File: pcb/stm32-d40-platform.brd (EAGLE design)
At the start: 99.1 x 99.1 mm, 84 parts, among them IC1 STM32F103C8, IC2 TODO AMIS30663CANG2G, IC3 STM32F103C8, J1 DIP-40, Q1 8MHz, Q2 8MHz, SW1 KSS-2EG4430, SW2 KSS-2EG4430, X1 DG3XX-03-3.5

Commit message: motherboard in progress
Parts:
- added 3V3, AVCC, PA0, PA1, PA10, PA11, PA12, PA13, PA14, PA15, PA2, PA3, PA4, PA5, PA6, PA7, PA8, PA9, PB0, PB1, PB10, PB11, PB12, PB13, PB14, PB15, PB2, PB3, PB4, PB5, PB6, PB7, PB8, PB9, PC14, PC15, RST, VBAT: (no value), pinhead-fixdrills:1X01
- added C23, C24: 22pF, rc-master-smd:C0603
- added G1: B2430, battery:B2430
- added IC4: (no value), transistor-arrays:SO16
- added K1, K2, K3, K4: ZNS5124, myrelays:ZN5
- added MOD1: STM32-MOD-CAN, stamp:DIL40
- added Q3: 32768Hz, crystal:TC38H-G
- added R36: 1M, rc-master-smd:R0603
- added SG1: F/QMBIII, buzzer:F/QMBIII
- added X2: DG3XX-12-5.0, degson:DG306-5.0-12P
- added X3: DG3XX-02-5.0, degson:DG306-5.0-02P
- moved U$1 58.4 mm to (93.6, 86.6)
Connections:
- new net !S2.RESET: MOD1.9, RST.1
- new net N$366: IC4.15, K4.A2
- new net N$367: IC4.14, K3.A2
- new net N$368: IC4.13, K2.A2
- new net N$369: IC4.12, K1.A2
- new net N$370: IC4.16, SG1.-
- new net N$64: K1.14, X2.1
- new net N$65: K1.11, X2.2
- new net N$66: K1.12, X2.3
- new net N$67: K2.14, X2.4
- new net N$68: K2.11, X2.5
- new net N$69: K2.12, X2.6
- new net N$70: K3.14, X2.7
- new net N$71: K3.11, X2.8
- new net N$72: K3.12, X2.9
- new net N$73: K4.14, X2.10
- new net N$74: K4.11, X2.11
- new net N$75: K4.12, X2.12
- new net S2.3V3: 3V3.1, MOD1.10
- new net S2.AVCC: AVCC.1, MOD1.30
- new net S2.OSC32_IN: C24.1, MOD1.13, PC14.1, Q3.2, R36.2
- new net S2.OSC32_OUT: C23.1, MOD1.12, PC15.1, Q3.1, R36.1
- new net S2.PA0: MOD1.40, PA0.1
- new net S2.PA1: MOD1.39, PA1.1
- new net S2.PA10: MOD1.24, PA10.1
- new net S2.PA11: MOD1.25, PA11.1
- new net S2.PA12: MOD1.26, PA12.1
- new net S2.PA13: MOD1.27, PA13.1
- new net S2.PA14: MOD1.28, PA14.1
- new net S2.PA15: MOD1.29, PA15.1
- new net S2.PA2: MOD1.38, PA2.1
- new net S2.PA3: MOD1.37, PA3.1
- new net S2.PA4: MOD1.36, PA4.1
- new net S2.PA5: MOD1.35, PA5.1
- new net S2.PA6: MOD1.34, PA6.1
- new net S2.PA7: MOD1.33, PA7.1
- new net S2.PA8: MOD1.22, PA8.1
- new net S2.PA9: MOD1.23, PA9.1
- new net S2.PB0: MOD1.1, PB0.1
- new net S2.PB1: MOD1.2, PB1.1
- new net S2.PB10: MOD1.16, PB10.1
- new net S2.PB11: MOD1.17, PB11.1
- new net S2.PB12: MOD1.18, PB12.1
- new net S2.PB13: MOD1.19, PB13.1
- new net S2.PB14: MOD1.20, PB14.1
- new net S2.PB15: MOD1.21, PB15.1
- new net S2.PB2: MOD1.3, PB2.1
- new net S2.PB3: MOD1.4, PB3.1
- new net S2.PB4: MOD1.5, PB4.1
- new net S2.PB5: MOD1.6, PB5.1
- new net S2.PB6: MOD1.7, PB6.1
- new net S2.PB7: MOD1.8, PB7.1
- new net S2.PB8: MOD1.14, PB8.1
- new net S2.PB9: MOD1.15, PB9.1
- new net S2.VBAT: G1.+, MOD1.32, VBAT.1
- net +5V: now also IC4.9, K1.A1, K2.A1, K3.A1, K4.A1, SG1.+, X3.2
- net GND: now also C23.2, C24.2, G1.-, IC4.8, MOD1.11, MOD1.31, Q3.GND, X3.1
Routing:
- net GND: track 5.08 -> 340.3 mm, vias 91 -> 144
- net S2.3V3: track 0.00 -> 257.6 mm, vias 0 -> 50
- net +5V: track 11.5 -> 77.2 mm
- net N$74: track 0.00 -> 30.8 mm
- net N$65: track 0.00 -> 30.8 mm
- net N$71: track 0.00 -> 28.1 mm
- net N$68: track 0.00 -> 28.1 mm
- net S2.OSC32_IN: track 0.00 -> 18.5 mm
- net N$75: track 0.00 -> 17.8 mm
- net S2.OSC32_OUT: track 0.00 -> 17.7 mm
- net N$64: track 0.00 -> 17.6 mm
- net N$73: track 0.00 -> 15.6 mm
- net N$66: track 0.00 -> 15.4 mm
- net N$72: track 0.00 -> 15.1 mm
- net N$67: track 0.00 -> 14.9 mm
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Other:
- outline, holes or cut-outs redrawn

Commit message: PCB ready
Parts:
- removed SG1: F/QMBIII, buzzer:F/QMBIII
- added C25, C26: 0.1, rc-master-smd:C0805
- added C27, C28: 100uF/6V3, rc-master:CE-035X080
- added D3: (no value), diodes:SMB
- added IN1, IN2, IN3, IN4, IN5, IN6, IN7, OUT5, OUT6, OUT7: (no value), pinhead-fixdrills:1X01
- added U2: (no value), vreg-linear:SOT223
- C23, C24: device rc-master-smd:C0603 -> rc-master-smd:C0805
- R36: device rc-master-smd:R0603 -> rc-master-smd:R0805
- moved U$1 21.7 mm to (72.4, 91.4)
- moved IC4 5.24 mm to (80.0, 69.8), turned to 0 degrees
- moved X3 2.54 mm to (85.1, 94.0)
- moved C23 0.63 mm to (34.3, 47.6)
- moved C24 0.63 mm to (36.8, 47.6)
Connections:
- removed net N$370: IC4.16, SG1.-
- new net HEAT: U2.4
- new net N$11: D3.A, X3.2
- new net S2.IN1: IC4.1, IN1.1
- new net S2.IN2: IC4.2, IN2.1
- new net S2.IN3: IC4.3, IN3.1
- new net S2.IN4: IC4.4, IN4.1
- new net S2.IN5: IC4.5, IN5.1
- new net S2.IN6: IC4.6, IN6.1
- new net S2.IN7: IC4.7, IN7.1
- new net S2.OUT5: IC4.12, OUT5.1
- new net S2.OUT6: IC4.11, OUT6.1
- new net S2.OUT7: IC4.10, OUT7.1
- net +5V: now also C25.1, C27.+, D3.C, U2.3; no longer SG1.+, X3.2
- net GND: now also C25.2, C26.2, C27.-, C28.-, U2.1
- net N$366: now also IC4.13; no longer IC4.15
- net N$368: now also IC4.15; no longer IC4.13
- net N$369: now also IC4.16; no longer IC4.12
- net S2.3V3: now also C26.1, C28.+, U2.2
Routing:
- net N$366: track 0.00 -> 80.5 mm, vias 0 -> 1
- net +5V: track 77.2 -> 143.7 mm, vias 1 -> 5
- net N$367: track 0.00 -> 60.4 mm, vias 0 -> 1
- net GND: track 340.3 -> 397.7 mm
- net S2.PB12: track 5.08 -> 45.7 mm, vias 0 -> 2
- net N$368: track 0.00 -> 40.3 mm, vias 0 -> 1
- net S2.PB14: track 5.08 -> 45.3 mm, vias 0 -> 2
- net S2.PB13: track 5.08 -> 44.5 mm, vias 0 -> 2
- net S2.PB15: track 5.08 -> 33.7 mm, vias 0 -> 2
- net S2.3V3: track 257.6 -> 280.1 mm, vias 50 -> 49
- net N$369: track 0.00 -> 20.2 mm, vias 0 -> 1
- net S2.OUT7: track 0.00 -> 12.5 mm
- net S2.OUT6: track 0.00 -> 11.8 mm
- net S2.OUT5: track 0.00 -> 11.7 mm
- net N$11: track 0.00 -> 8.22 mm
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- added copper zone on layer 1, net HEAT
- added copper zone on layer 16, net HEAT

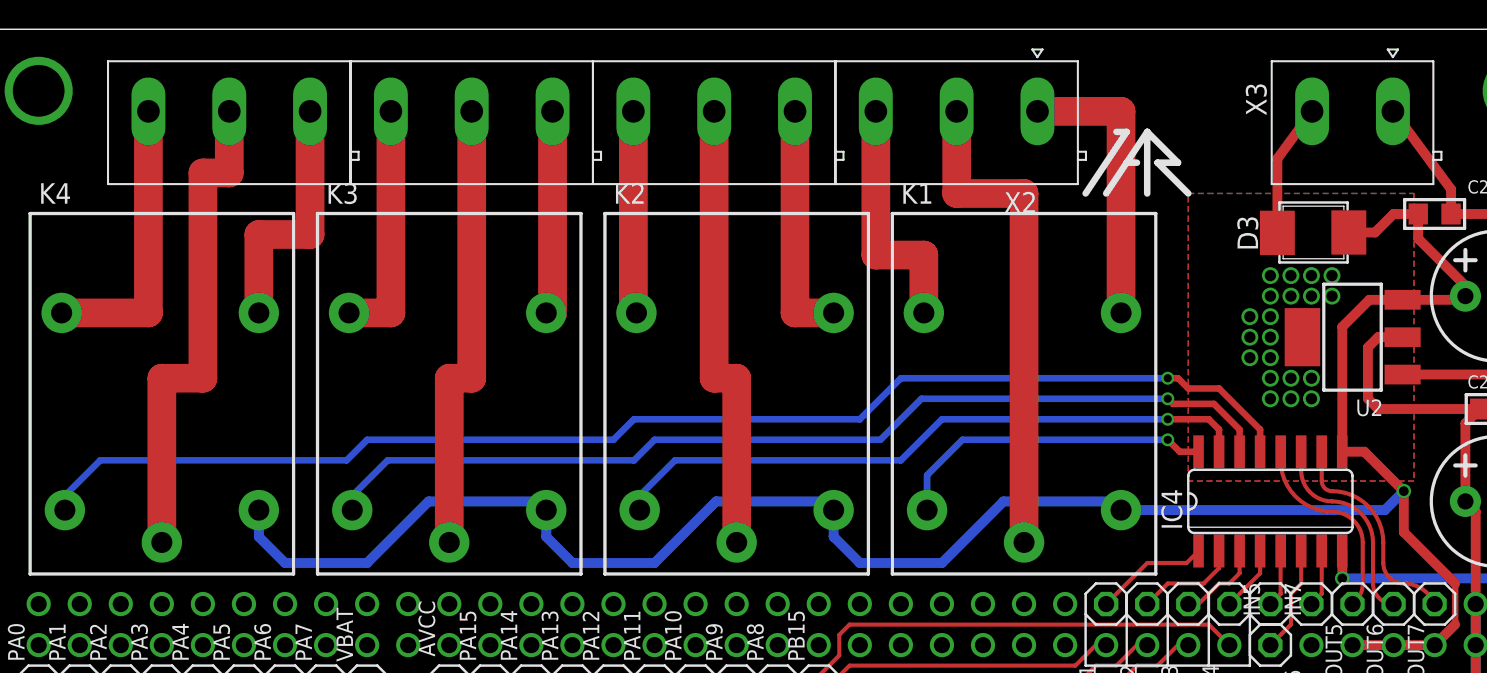
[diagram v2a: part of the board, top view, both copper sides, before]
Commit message: stm32-40 ready to production PCB. some changes in platform
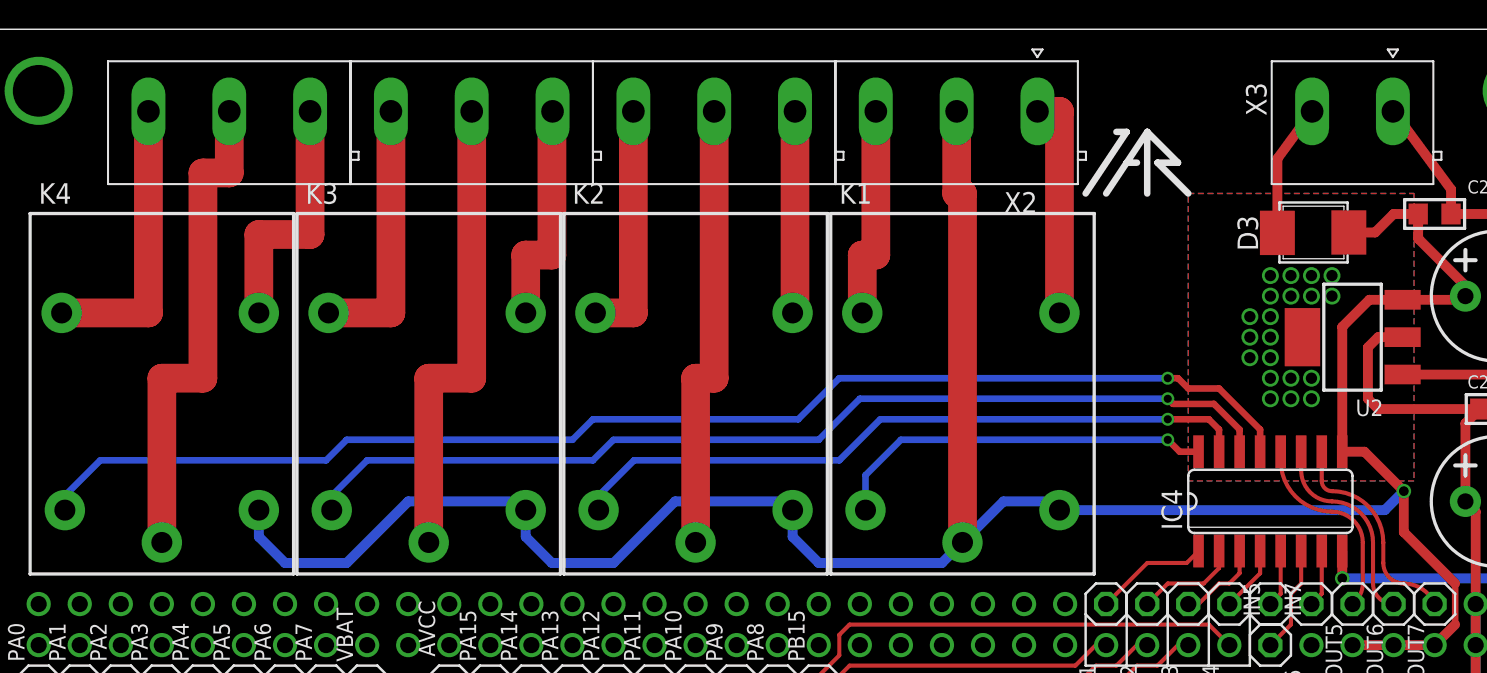
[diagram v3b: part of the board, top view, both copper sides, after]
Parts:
- moved K1 3.81 mm to (61.0, 76.2)
- moved K2 2.54 mm to (44.5, 76.2)
- moved K3 1.27 mm to (27.9, 76.2)
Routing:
- net N$64: track 17.6 -> 13.8 mm
- net N$369: track 20.2 -> 24.0 mm
- net N$65: track 30.8 -> 27.0 mm
- net N$368: track 40.3 -> 42.9 mm
- net N$67: track 14.9 -> 12.6 mm
- net N$69: track 12.7 -> 14.8 mm
- net N$66: track 15.4 -> 13.3 mm
- net N$72: track 15.1 -> 16.3 mm
- net N$70: track 12.9 -> 14.1 mm
- net N$71: track 28.1 -> 29.3 mm
- net N$367: track 60.4 -> 61.7 mm

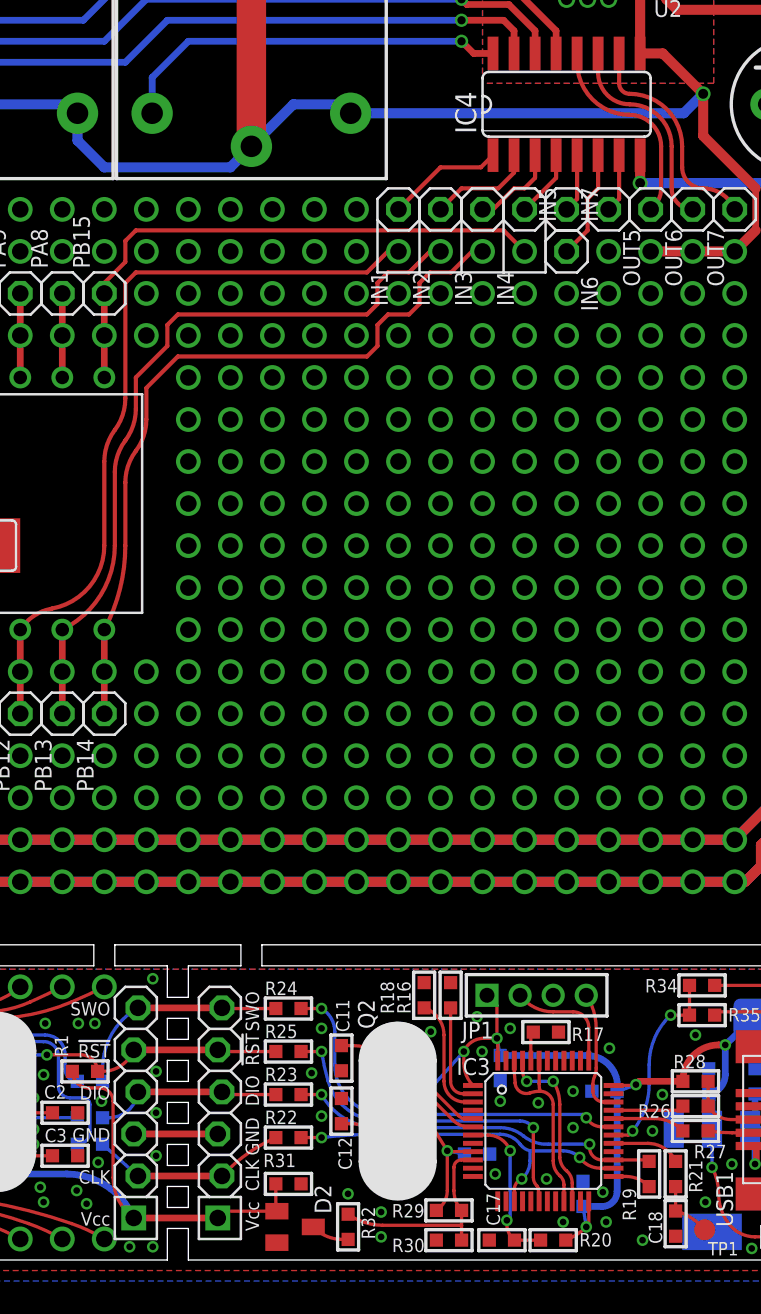
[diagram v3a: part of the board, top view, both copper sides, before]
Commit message: ST-link v2 SWD some fixes
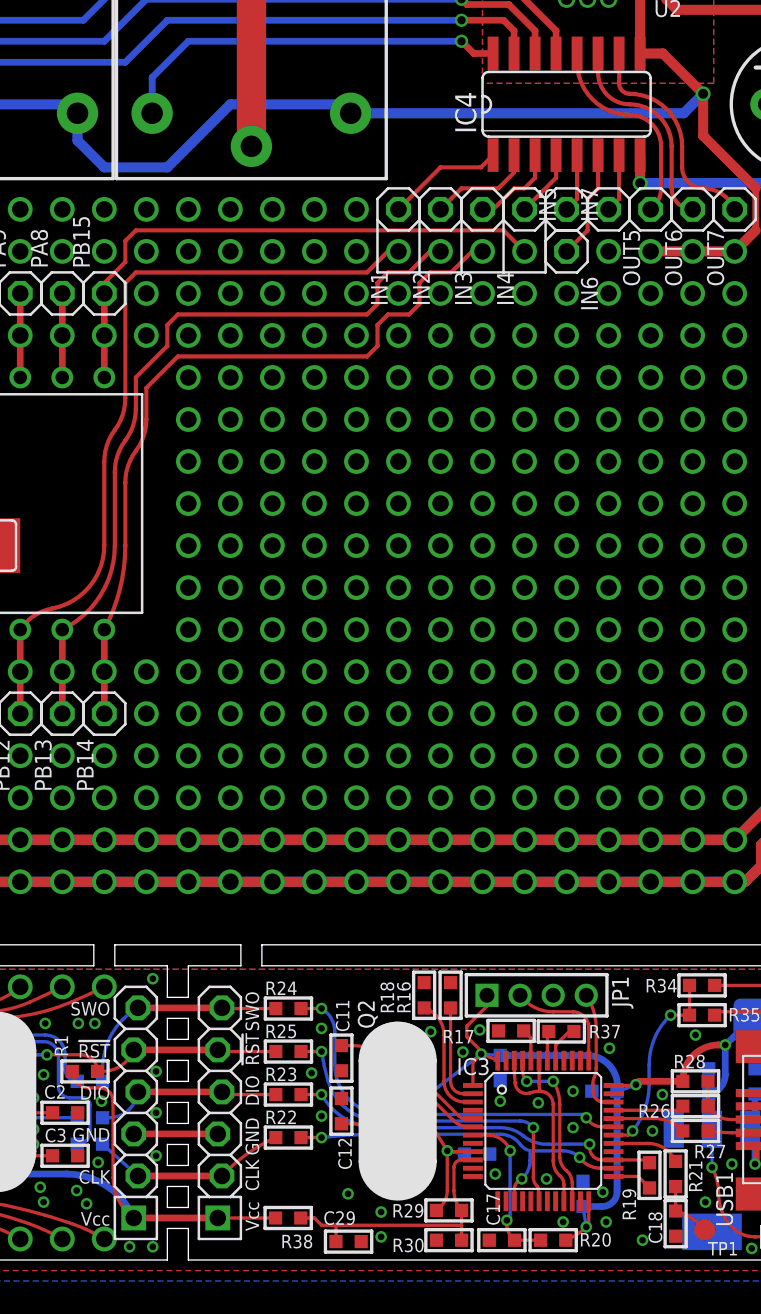
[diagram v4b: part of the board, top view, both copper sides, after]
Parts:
- removed D2: (no value), diodes:SOT23
- removed R31: 10K, rc-master-smd:R0603
- removed R32: 100, rc-master-smd:R0603
- added C29: 0.01, rc-master-smd:C0603
- added R37: 220, rc-master-smd:R0603
- added R38: 4.7K, rc-master-smd:R0603
- R19: value 100 -> 220
- R26, R27: value 0 -> 22
- R34, R35: value 100 -> 510
- moved R17 2.10 mm to (76.7, 13.8), turned to 0 degrees
- moved R19 0.08 mm to (85.0, 5.12), turned to 270 degrees
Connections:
- removed net N$49: D2.3, R32.2
- new net S3.M25_CS: IC3.11
- new net S3.U2_CK: IC3.14
- new net S3.U2_RX: IC3.13
- new net S3.U2_TX: IC3.12
- net +3V3: now also R38.2; no longer D2.1, R31.1
- net GND: now also C29.2; no longer R31.2
- net S3.AIN1: now also C29.1, R38.1; no longer R32.1
- net S3.SWIM_RST: now also R37.2
- net S3.SWIM_RST_IN: now also R37.1
- net S3.T_JTMS: now also R19.1; no longer R19.2
- net S3.T_SWDIO_IN: now also R19.2; no longer R19.1
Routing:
- net S3.AIN1: track 12.8 -> 16.7 mm
- net S3.SWIM_RST_IN: track 0.00 -> 2.39 mm
- net N$49: track 2.26 -> 0.00 mm
- net +3V3: track 103.0 -> 101.1 mm
- net S3.SWIM_RST: track 0.00 -> 1.79 mm
- net VCC: track 77.1 -> 76.9 mm, vias 9 -> 8
- net GND: vias 144 -> 143
